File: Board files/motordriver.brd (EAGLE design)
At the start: 30.2 x 44.5 mm, 13 parts, among them Q1 IPB034N03L, U1 VNH5019A

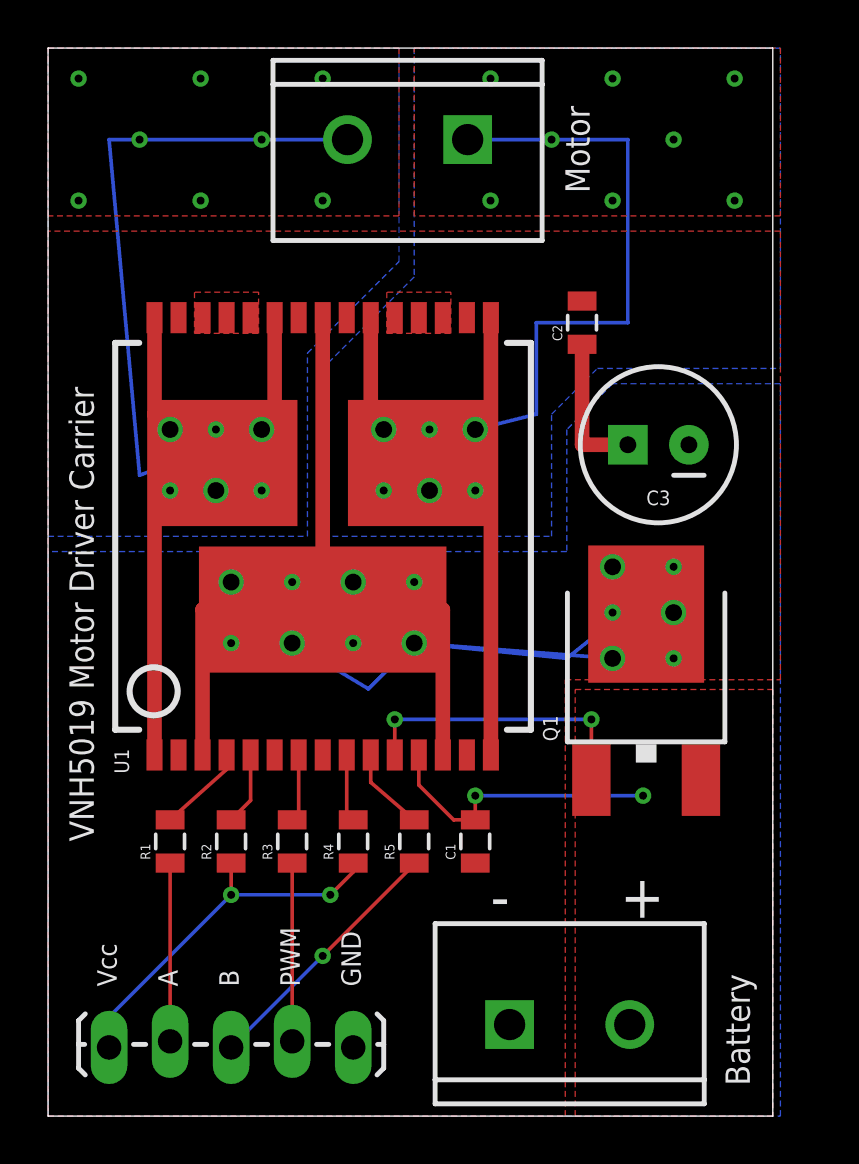
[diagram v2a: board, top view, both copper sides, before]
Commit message: Made silkscreen orientation consistent
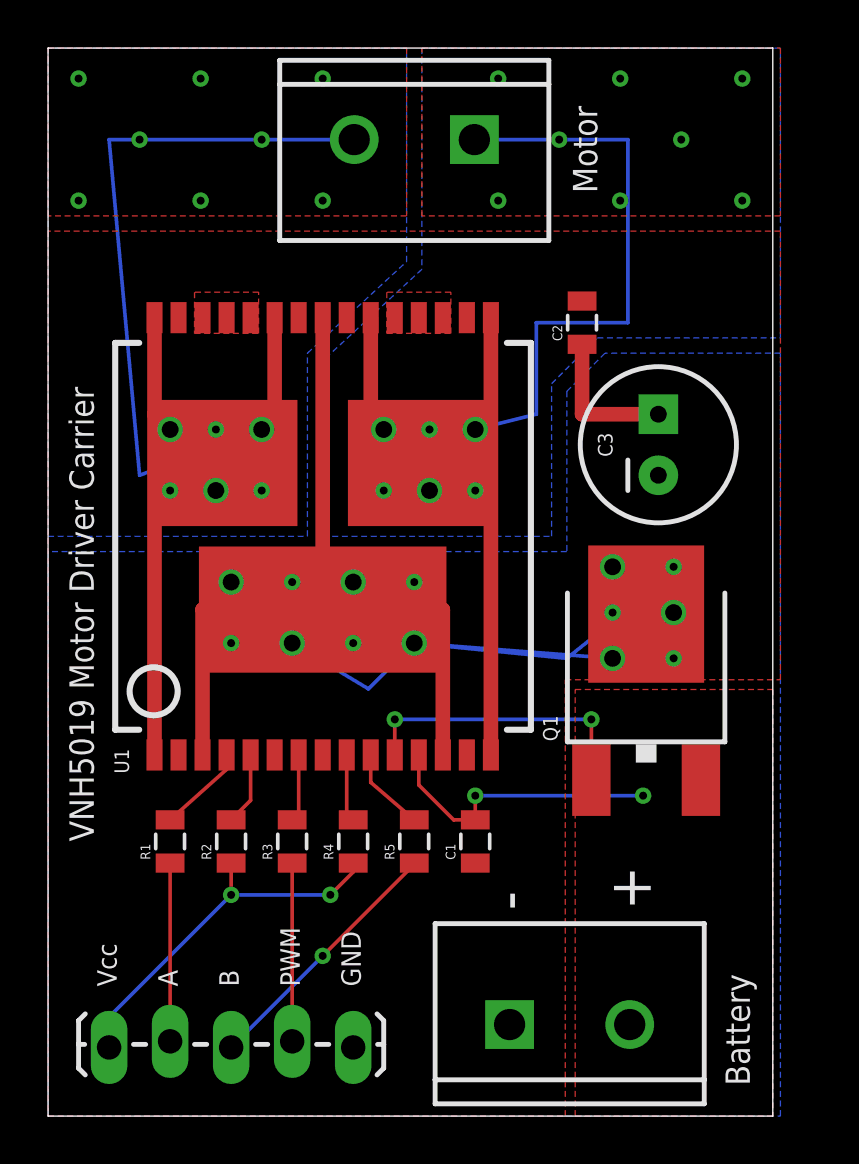
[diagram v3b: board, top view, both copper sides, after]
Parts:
- moved JP3 0.28 mm to (17.7, 40.6)
- turned C3 to 90 degrees
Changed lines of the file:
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@@
 <wire x1="0" y1="44.45" x2="0" y2="0" width="0" layer="20"/>
 <text x="1.905" y="11.43" size="1.016" layer="21" rot="R90">VNH5019 Motor Driver Carrier</text>
-<text x="23.8125" y="8.255" size="1.778" layer="21">+</text>
-<text x="18.415" y="8.255" size="1.778" layer="21">-</text>
+<text x="25.0825" y="8.5725" size="1.778" layer="21" rot="R90">+</text>
+<text x="20.0025" y="8.5725" size="1.778" layer="21" rot="R90">-</text>
 <text x="2.8575" y="5.3975" size="0.8128" layer="21" rot="R90">Vcc</text>
 <text x="5.3975" y="5.3975" size="0.8128" layer="21" rot="R90">A</text>
@@
 <text x="13.0175" y="5.3975" size="0.8128" layer="21" rot="R90">GND</text>
 <text x="29.21" y="1.27" size="1.016" layer="21" rot="R90">Battery</text>
-<text x="22.5425" y="38.4175" size="1.016" layer="21" rot="R90">Motor</text>
+<text x="22.86" y="38.4175" size="1.016" layer="21" rot="R90">Motor</text>
 </plain>
 <attributes>
@@
 <attribute name="VALUE" x="13.97" y="6.1595" size="1.27" layer="27" font="vector" rot="R180"/>
 </element>
-<element name="JP3" library="SparkFun-Connectors" package="SCREWTERMINAL-5MM-2" value="MOTOR" x="17.4625" y="40.64" smashed="yes" rot="R180"/>
+<element name="JP3" library="SparkFun-Connectors" package="SCREWTERMINAL-5MM-2" value="MOTOR" x="17.7419" y="40.64" smashed="yes" rot="R180"/>
 <element name="Q1" library="SparkFun-DiscreteSemi" package="DPAK" value="IPB034N03L" x="24.892" y="19.304" smashed="yes">
 <attribute name="PROD_ID" value="TRANS-09984" x="24.892" y="19.304" size="1.778" layer="27" display="off"/>
@@
 <element name="C1" library="SparkFun-Capacitors" package="0805" value="0.1uF" x="17.78" y="11.43" rot="R90"/>
 <element name="C2" library="SparkFun-Capacitors" package="0805" value="0.1uF" x="22.225" y="33.02" rot="R90"/>
-<element name="C3" library="SparkFun-Capacitors" package="CPOL-RADIAL-100UF-25V" value="47uF" x="25.4" y="27.94" smashed="yes" rot="R180">
-<attribute name="NAME" x="25.4" y="26.035" size="0.6096" layer="25" rot="R180" align="bottom-center"/>
+<element name="C3" library="SparkFun-Capacitors" package="CPOL-RADIAL-100UF-25V" value="47uF" x="25.4" y="27.94" smashed="yes" rot="R90">
+<attribute name="NAME" x="23.495" y="27.94" size="0.6096" layer="25" rot="R90" align="bottom-center"/>
 </element>
 <element name="R1" library="SparkFun-Resistors" package="0805" value="1k" x="5.08" y="11.43" rot="R90"/>
@@
 <vertex x="11.43" y="24.13"/>
 <vertex x="20.955" y="24.13"/>
-<vertex x="20.955" y="29.21"/>
-<vertex x="22.86" y="31.115"/>
-<vertex x="30.48" y="31.115"/>
+<vertex x="20.955" y="30.48"/>
+<vertex x="22.86" y="32.385"/>
+<vertex x="30.48" y="32.385"/>
 <vertex x="30.48" y="44.45"/>
-<vertex x="15.24" y="44.45"/>
-<vertex x="15.24" y="34.925"/>
-<vertex x="11.43" y="31.115"/>
+<vertex x="15.5575" y="44.45"/>
+<vertex x="15.5575" y="35.2425"/>
+<vertex x="11.43" y="31.4325"/>
 </polygon>
 <wire x1="15.595" y1="27.18" x2="15.595" y2="27.94" width="0.1524" layer="1"/>
@@
 <wire x1="20.32" y1="33.02" x2="24.13" y2="33.02" width="0.1524" layer="16"/>
 <wire x1="24.13" y1="33.02" x2="24.13" y2="40.64" width="0.1524" layer="16"/>
-<wire x1="24.13" y1="40.64" x2="20.955" y2="40.64" width="0.1524" layer="16"/>
-<wire x1="20.955" y1="40.64" x2="17.4625" y2="40.64" width="0.1524" layer="16"/>
+<wire x1="24.13" y1="40.64" x2="21.2725" y2="40.64" width="0.1524" layer="16"/>
+<wire x1="21.2725" y1="40.64" x2="17.7419" y2="40.64" width="0.1524" layer="16"/>
 <wire x1="18.43" y1="33.23" x2="18.43" y2="15.03" width="0.6096" layer="1"/>
 <wire x1="18.43" y1="33.23" x2="18.43" y2="29.21" width="0.1524" layer="1"/>
@@
 <vertex x="30.48" y="44.45"/>
 <vertex x="30.48" y="37.465"/>
-<vertex x="15.24" y="37.465"/>
-<vertex x="15.24" y="44.45"/>
-</polygon>
-<via x="20.955" y="40.64" extent="1-16" drill="0.3302"/>
+<vertex x="15.5575" y="37.465"/>
+<vertex x="15.5575" y="44.45"/>
+</polygon>
+<via x="21.2725" y="40.64" extent="1-16" drill="0.3302"/>
 <via x="13.97" y="26.035" extent="1-16" drill="0.3302"/>
-<via x="28.575" y="43.18" extent="1-16" drill="0.3302"/>
-<via x="28.575" y="38.1" extent="1-16" drill="0.3302"/>
-<via x="26.035" y="40.64" extent="1-16" drill="0.3302"/>
-<via x="23.495" y="38.1" extent="1-16" drill="0.3302"/>
-<via x="23.495" y="43.18" extent="1-16" drill="0.3302"/>
-<via x="18.415" y="43.18" extent="1-16" drill="0.3302"/>
-<via x="18.415" y="38.1" extent="1-16" drill="0.3302"/>
+<via x="28.8925" y="43.18" extent="1-16" drill="0.3302"/>
+<via x="28.8925" y="38.1" extent="1-16" drill="0.3302"/>
+<via x="26.3525" y="40.64" extent="1-16" drill="0.3302"/>
+<via x="23.8125" y="38.1" extent="1-16" drill="0.3302"/>
+<via x="23.8125" y="43.18" extent="1-16" drill="0.3302"/>
+<via x="18.7325" y="43.18" extent="1-16" drill="0.3302"/>
+<via x="18.7325" y="38.1" extent="1-16" drill="0.3302"/>
 <via x="15.875" y="28.575" extent="1-16" drill="0.3302"/>
 <via x="17.78" y="26.035" extent="1-16" drill="0.3302"/>
@@
 <vertex x="10.795" y="24.13"/>
 <vertex x="10.795" y="31.75"/>
-<vertex x="14.605" y="35.56"/>
-<vertex x="14.605" y="44.45"/>
+<vertex x="14.9225" y="35.56"/>
+<vertex x="14.9225" y="44.45"/>
 <vertex x="0" y="44.45"/>
 </polygon>
@@
 <wire x1="2.54" y1="40.64" x2="3.81" y2="40.64" width="0.1524" layer="16"/>
 <wire x1="3.81" y1="40.64" x2="8.89" y2="40.64" width="0.1524" layer="16"/>
-<wire x1="8.89" y1="40.64" x2="12.4625" y2="40.64" width="0.1524" layer="16"/>
+<wire x1="8.89" y1="40.64" x2="12.7419" y2="40.64" width="0.1524" layer="16"/>
 <wire x1="4.43" y1="33.23" x2="4.43" y2="29.21" width="0.6096" layer="1"/>
 <wire x1="4.43" y1="29.21" x2="4.43" y2="15.03" width="0.6096" layer="1"/>
@@
 <polygon width="0.3048" layer="1">
 <vertex x="0" y="44.45"/>
-<vertex x="14.605" y="44.45"/>
-<vertex x="14.605" y="37.465"/>
+<vertex x="14.9225" y="44.45"/>
+<vertex x="14.9225" y="37.465"/>
 <vertex x="0" y="37.465"/>
 </polygon>
@@
 <wire x1="11.43" y1="21.08" x2="8.13" y2="21.08" width="0.1524" layer="1"/>
 <wire x1="8.13" y1="21.08" x2="7.62" y2="21.59" width="0.1524" layer="1"/>
-<wire x1="22.225" y1="32.12" x2="22.225" y2="27.94" width="0.6096" layer="1"/>
-<wire x1="22.225" y1="27.94" x2="24.13" y2="27.94" width="0.6096" layer="1"/>
+<wire x1="22.225" y1="32.12" x2="22.225" y2="29.21" width="0.6096" layer="1"/>
+<wire x1="22.225" y1="29.21" x2="25.4" y2="29.21" width="0.6096" layer="1"/>
 <polygon width="0.254" layer="16">
 <vertex x="0" y="0"/>
 <vertex x="30.48" y="0"/>
-<vertex x="30.48" y="30.48"/>
-<vertex x="23.495" y="30.48"/>
-<vertex x="21.59" y="28.575"/>
+<vertex x="30.48" y="31.75"/>
+<vertex x="23.1775" y="31.75"/>
+<vertex x="21.59" y="30.1625"/>
 <vertex x="21.59" y="23.495"/>
 <vertex x="0" y="23.495"/>

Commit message: Cleaned up wires on motor driver board
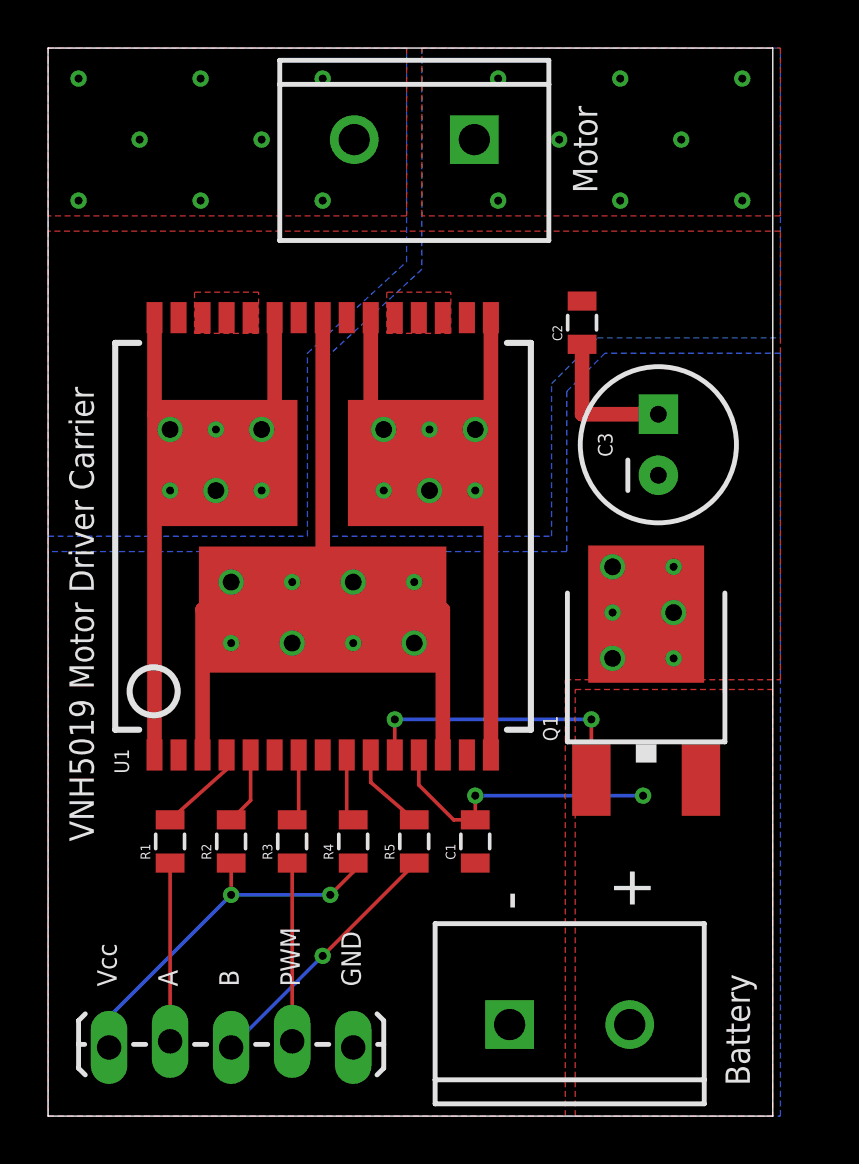
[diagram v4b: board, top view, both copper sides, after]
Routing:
- net VCC: track 97.7 -> 61.5 mm
- net OUTA: track 70.3 -> 35.5 mm
- net OUTB: track 71.2 -> 41.7 mm
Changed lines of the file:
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@@
 <wire x1="15.595" y1="28.575" x2="13.97" y2="28.575" width="0.1524" layer="1"/>
 <via x="13.97" y="28.575" extent="1-16" drill="0.7"/>
-<wire x1="13.97" y1="28.575" x2="13.97" y2="26.035" width="0.1524" layer="16"/>
-<wire x1="13.97" y1="26.035" x2="13.97" y2="25.4" width="0.1524" layer="16"/>
-<wire x1="13.97" y1="25.4" x2="15.875" y2="26.035" width="0.1524" layer="16"/>
 <via x="15.875" y="26.035" extent="1-16" drill="0.7"/>
 <wire x1="15.875" y1="26.035" x2="15.24" y2="29.21" width="0.1524" layer="1"/>
 <wire x1="15.24" y1="29.21" x2="17.78" y2="28.575" width="0.1524" layer="1"/>
 <via x="17.78" y="28.575" extent="1-16" drill="0.7"/>
-<wire x1="17.78" y1="28.575" x2="20.32" y2="29.21" width="0.1524" layer="16"/>
-<wire x1="20.32" y1="29.21" x2="20.32" y2="33.02" width="0.1524" layer="16"/>
-<wire x1="20.32" y1="33.02" x2="24.13" y2="33.02" width="0.1524" layer="16"/>
-<wire x1="24.13" y1="33.02" x2="24.13" y2="40.64" width="0.1524" layer="16"/>
-<wire x1="24.13" y1="40.64" x2="21.2725" y2="40.64" width="0.1524" layer="16"/>
-<wire x1="21.2725" y1="40.64" x2="17.7419" y2="40.64" width="0.1524" layer="16"/>
 <wire x1="18.43" y1="33.23" x2="18.43" y2="15.03" width="0.6096" layer="1"/>
 <wire x1="18.43" y1="33.23" x2="18.43" y2="29.21" width="0.1524" layer="1"/>
@@
 <wire x1="7.265" y1="29.21" x2="5.08" y2="28.575" width="0.1524" layer="1"/>
 <via x="5.08" y="28.575" extent="1-16" drill="0.7"/>
-<wire x1="5.08" y1="28.575" x2="5.08" y2="26.035" width="0.1524" layer="16"/>
-<wire x1="5.08" y1="25.4" x2="6.985" y2="26.035" width="0.1524" layer="16"/>
 <via x="6.985" y="26.035" extent="1-16" drill="0.7"/>
 <wire x1="6.985" y1="26.035" x2="6.35" y2="29.21" width="0.1524" layer="1"/>
 <wire x1="6.35" y1="29.21" x2="8.89" y2="28.575" width="0.1524" layer="1"/>
 <via x="8.89" y="28.575" extent="1-16" drill="0.7"/>
-<wire x1="8.89" y1="28.575" x2="3.81" y2="26.67" width="0.1524" layer="16"/>
-<wire x1="3.81" y1="26.67" x2="2.54" y2="40.64" width="0.1524" layer="16"/>
-<wire x1="2.54" y1="40.64" x2="3.81" y2="40.64" width="0.1524" layer="16"/>
-<wire x1="3.81" y1="40.64" x2="8.89" y2="40.64" width="0.1524" layer="16"/>
-<wire x1="8.89" y1="40.64" x2="12.7419" y2="40.64" width="0.1524" layer="16"/>
 <wire x1="4.43" y1="33.23" x2="4.43" y2="29.21" width="0.6096" layer="1"/>
 <wire x1="4.43" y1="29.21" x2="4.43" y2="15.03" width="0.6096" layer="1"/>
@@
 <via x="3.81" y="40.64" extent="1-16" drill="0.3302"/>
 <via x="8.89" y="40.64" extent="1-16" drill="0.3302"/>
-<wire x1="5.08" y1="26.035" x2="5.08" y2="25.4" width="0.1524" layer="16"/>
 <via x="5.08" y="26.035" extent="1-16" drill="0.3302"/>
 <via x="8.89" y="26.035" extent="1-16" drill="0.3302"/>
@@
 <wire x1="26.162" y1="21.463" x2="23.495" y2="22.86" width="0.1524" layer="1"/>
 <via x="23.495" y="22.86" extent="1-16" drill="0.7"/>
-<wire x1="23.495" y1="22.86" x2="25.4" y2="22.86" width="0.1524" layer="16"/>
-<wire x1="25.4" y1="22.86" x2="26.035" y2="20.955" width="0.1524" layer="16"/>
 <via x="26.035" y="20.955" extent="1-16" drill="0.7"/>
 <wire x1="26.035" y1="20.955" x2="26.67" y2="20.955" width="0.1524" layer="1"/>
 <wire x1="26.67" y1="20.955" x2="23.495" y2="19.05" width="0.1524" layer="1"/>
 <via x="23.495" y="19.05" extent="1-16" drill="0.7"/>
-<wire x1="23.495" y1="19.05" x2="15.24" y2="19.685" width="0.1524" layer="16"/>
-<wire x1="15.24" y1="19.685" x2="13.335" y2="17.78" width="0.1524" layer="16"/>
-<wire x1="13.335" y1="17.78" x2="10.16" y2="19.685" width="0.1524" layer="16"/>
 <via x="7.62" y="22.225" extent="1-16" drill="0.7"/>
-<wire x1="10.16" y1="19.685" x2="7.62" y2="22.225" width="0.1524" layer="16"/>
 <wire x1="7.62" y1="22.225" x2="7.62" y2="21.59" width="0.1524" layer="1"/>
 <wire x1="7.62" y1="21.59" x2="10.16" y2="19.685" width="0.1524" layer="1"/>
 <via x="10.16" y="19.685" extent="1-16" drill="0.7"/>
-<wire x1="10.16" y1="19.685" x2="12.7" y2="22.225" width="0.1524" layer="16"/>
 <via x="12.7" y="22.225" extent="1-16" drill="0.7"/>
 <wire x1="12.7" y1="22.225" x2="12.065" y2="21.59" width="0.1524" layer="1"/>
 <wire x1="12.065" y1="21.59" x2="15.24" y2="19.685" width="0.1524" layer="1"/>
 <via x="15.24" y="19.685" extent="1-16" drill="0.7"/>
-<wire x1="15.24" y1="19.685" x2="21.59" y2="19.05" width="0.1524" layer="16"/>
-<wire x1="21.59" y1="19.05" x2="24.765" y2="21.59" width="0.1524" layer="16"/>
 <wire x1="11.43" y1="21.08" x2="8.13" y2="21.08" width="0.1524" layer="1"/>
 <wire x1="8.13" y1="21.08" x2="7.62" y2="21.59" width="0.1524" layer="1"/>

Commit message: Switched to polarized connectors
Also added 3.3v out pins on logic board, various other changes
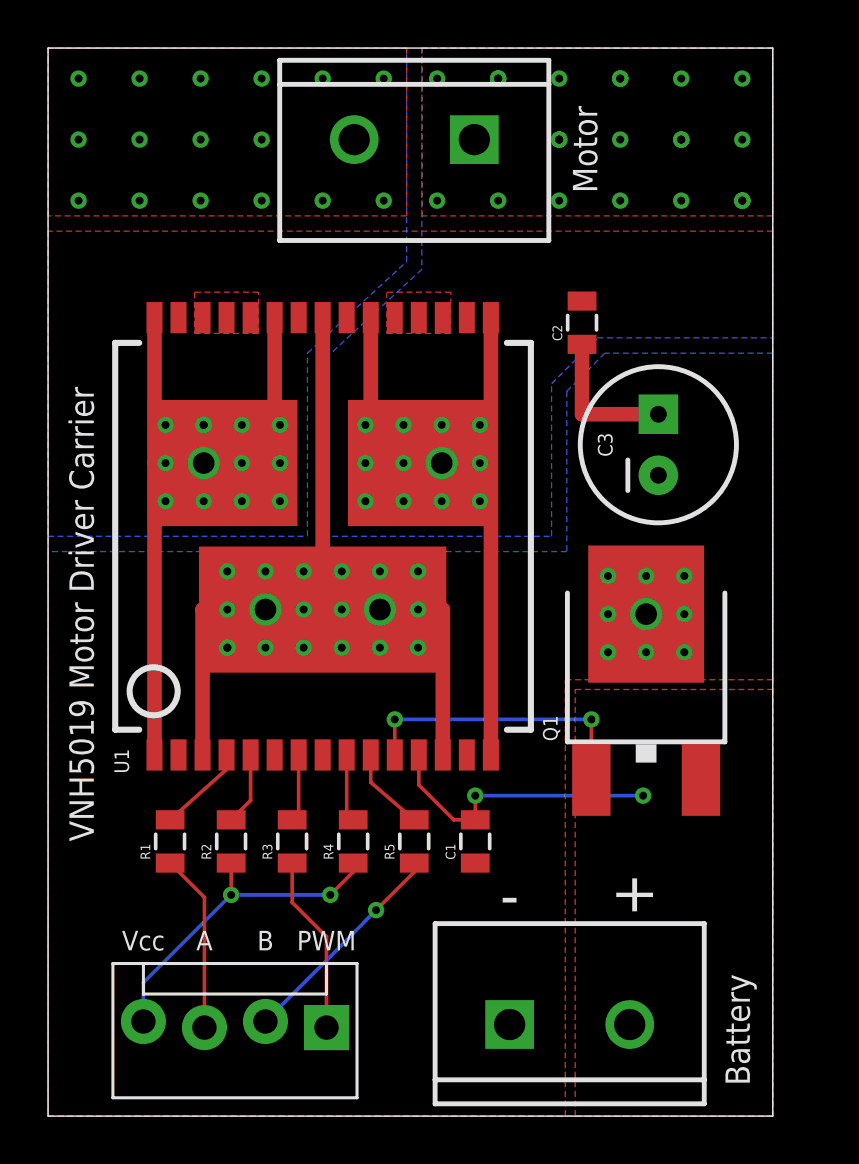
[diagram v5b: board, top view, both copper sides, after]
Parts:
- JP1: device SparkFun-Connectors:1X05_LOCK_LONGPADS -> SparkFun-Connectors:MOLEX-1X4_LOCK
- moved JP1 1.46 mm to (11.6, 3.81)
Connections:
- net 3.3V: now also JP1.4; no longer JP1.5
- net GND: no longer JP1.1
- net N$5: now also JP1.2; no longer JP1.3
- net N$7: now also JP1.3; no longer JP1.4
- net N$8: now also JP1.1; no longer JP1.2
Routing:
- net VCC: track 61.5 -> 43.8 mm, vias 14 -> 28
- net OUTB: track 41.7 -> 30.9 mm, vias 14 -> 33
- net OUTA: track 35.5 -> 28.9 mm, vias 14 -> 29
- net N$5: track 10.8 -> 9.15 mm
- net 3.3V: track 15.6 -> 13.9 mm
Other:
- board text removed: "GND"
